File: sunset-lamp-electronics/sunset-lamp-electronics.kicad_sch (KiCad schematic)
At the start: 30 parts

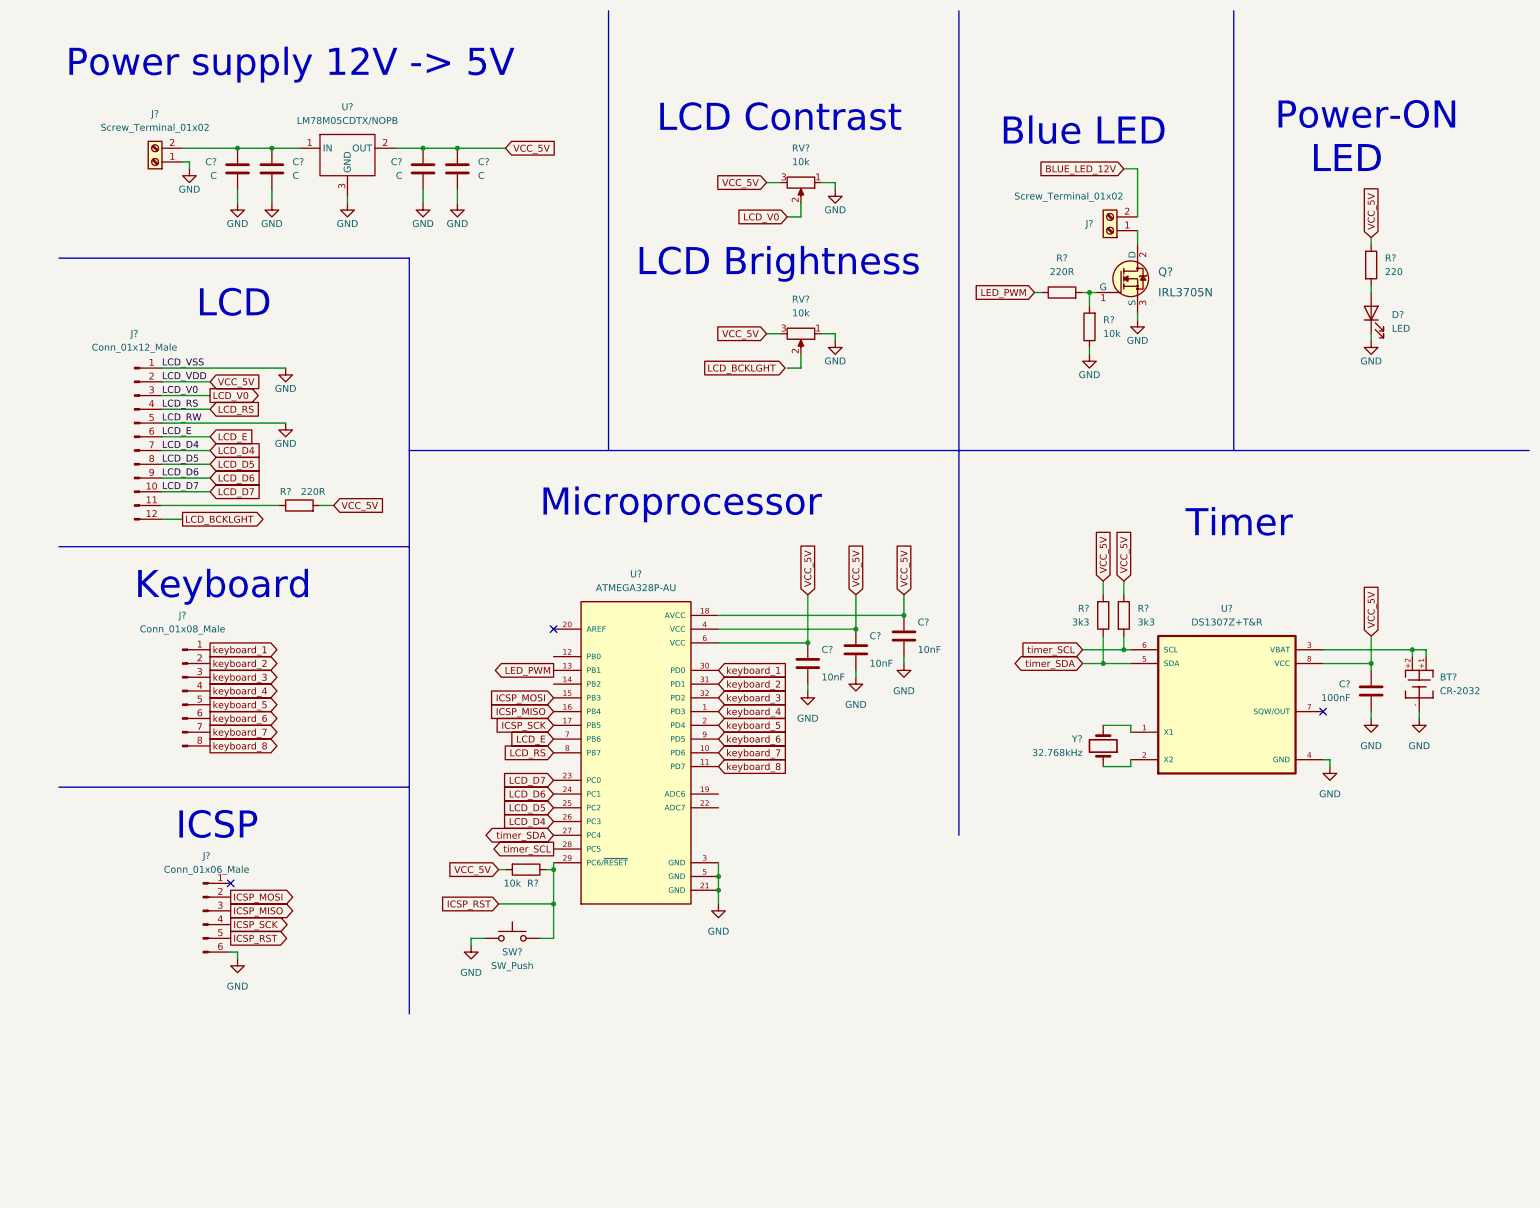
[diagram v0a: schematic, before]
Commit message: Finished schematics and added footprints to all components
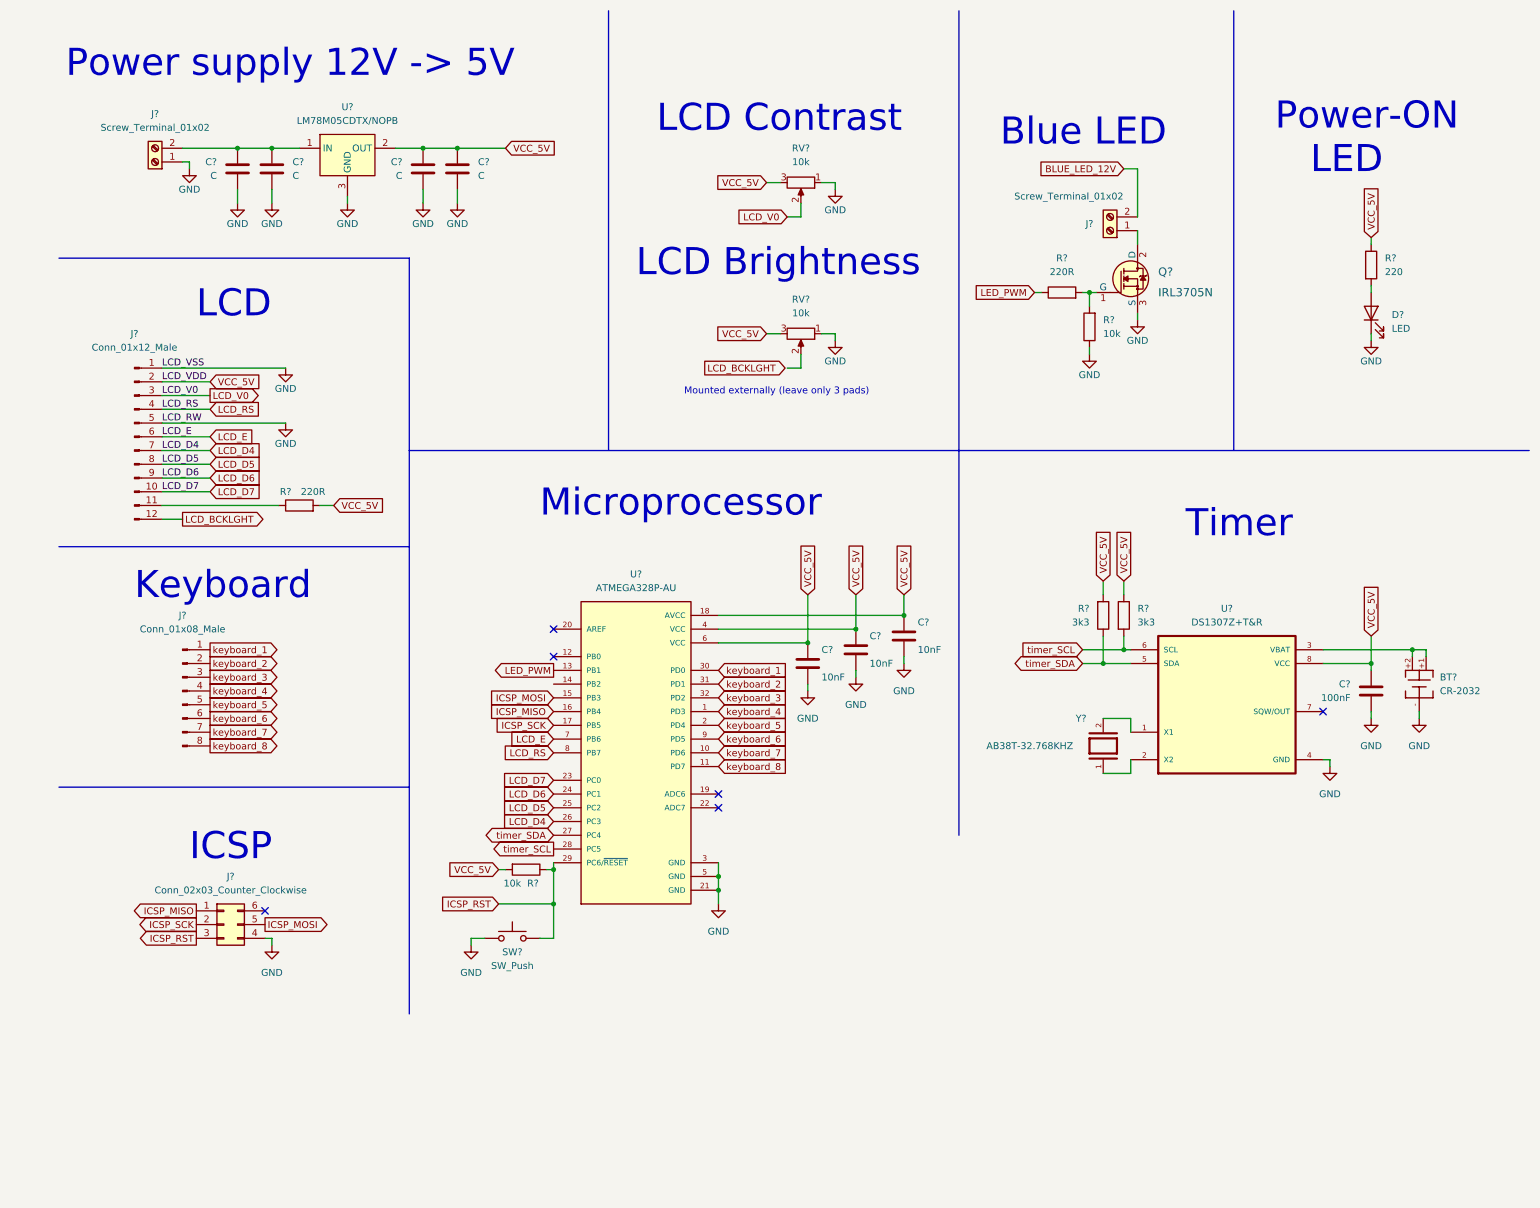
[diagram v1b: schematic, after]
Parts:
- removed J?: Conn_01x06_Male, symbol Connector:Conn_01x06_Male
- removed U?: LM78M05CDTX/NOPB, symbol iridiumLinearVoltageRegulators:LM78M05CDTX/NOPB
- removed Y?: 32.768kHz, symbol Device:Crystal
- added J?: Conn_02x03_Counter_Clockwise, Connector_PinHeader_2.54mm:PinHeader_2x03_P2.54mm_Vertical, symbol Connector_Generic:Conn_02x03_Counter_Clockwise
- added U?: LM78M05CDTX/NOPB, iridium-footprints:TO-252-DPAK, symbol iridiumLinearVoltageRegulators:LM78M05CDTX/NOPB
- added Y?: AB38T-32.768KHZ, iridium-footprints:XTAL_AB38T-32.768KHZ, symbol iridiumOscillators:AB38T-32.768KHZ
- D?: footprint (none) -> LED_SMD:LED_0805_2012Metric_Pad1.15x1.40mm_HandSolder
- J?: footprint (none) -> Connector_PinHeader_2.54mm:PinHeader_1x12_P2.54mm_Vertical
- J? (x2): footprint (none) -> TerminalBlock:TerminalBlock_Altech_AK300-2_P5.00mm
- J?: footprint (none) -> Connector_PinHeader_2.54mm:PinHeader_1x08_P2.54mm_Vertical
- Q?: footprint (none) -> iridium-footprints:TO-220
- RV?: footprint (none) -> iridium-footprints:TrimmPotentiometer
- RV?: footprint (none) -> Connector_PinHeader_2.54mm:PinHeader_1x03_P2.54mm_Vertical
- SW?: footprint (none) -> Button_Switch_THT:SW_PUSH_6mm_H5mm
- U?: footprint QFP80P900X900X120-32N -> iridium-footprints:TQFP-32
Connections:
- net GND: now also J?.4 (Pin_4), U?.3 (GND)
- net ICSP_MISO: now also J?.1 (Pin_1)
- net ICSP_MOSI: now also J?.5 (Pin_5)
- net ICSP_RST: now also J?.3 (Pin_3)
- net ICSP_SCK: now also J?.2 (Pin_2)
- net VCC_5V: now also U?.2 (OUT)
- net at U?.1 (X1): now also Y?.2
- net at U?.2 (X2): now also Y?.1
- net at C?.1, C?.2, J?.2 (Pin_2): now also U?.1 (IN)
- no-connect marks 3 -> 6
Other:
- note added: "Mounted externally (leave only 3 pads)"

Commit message: Corrected R and C symbols and performed ERC
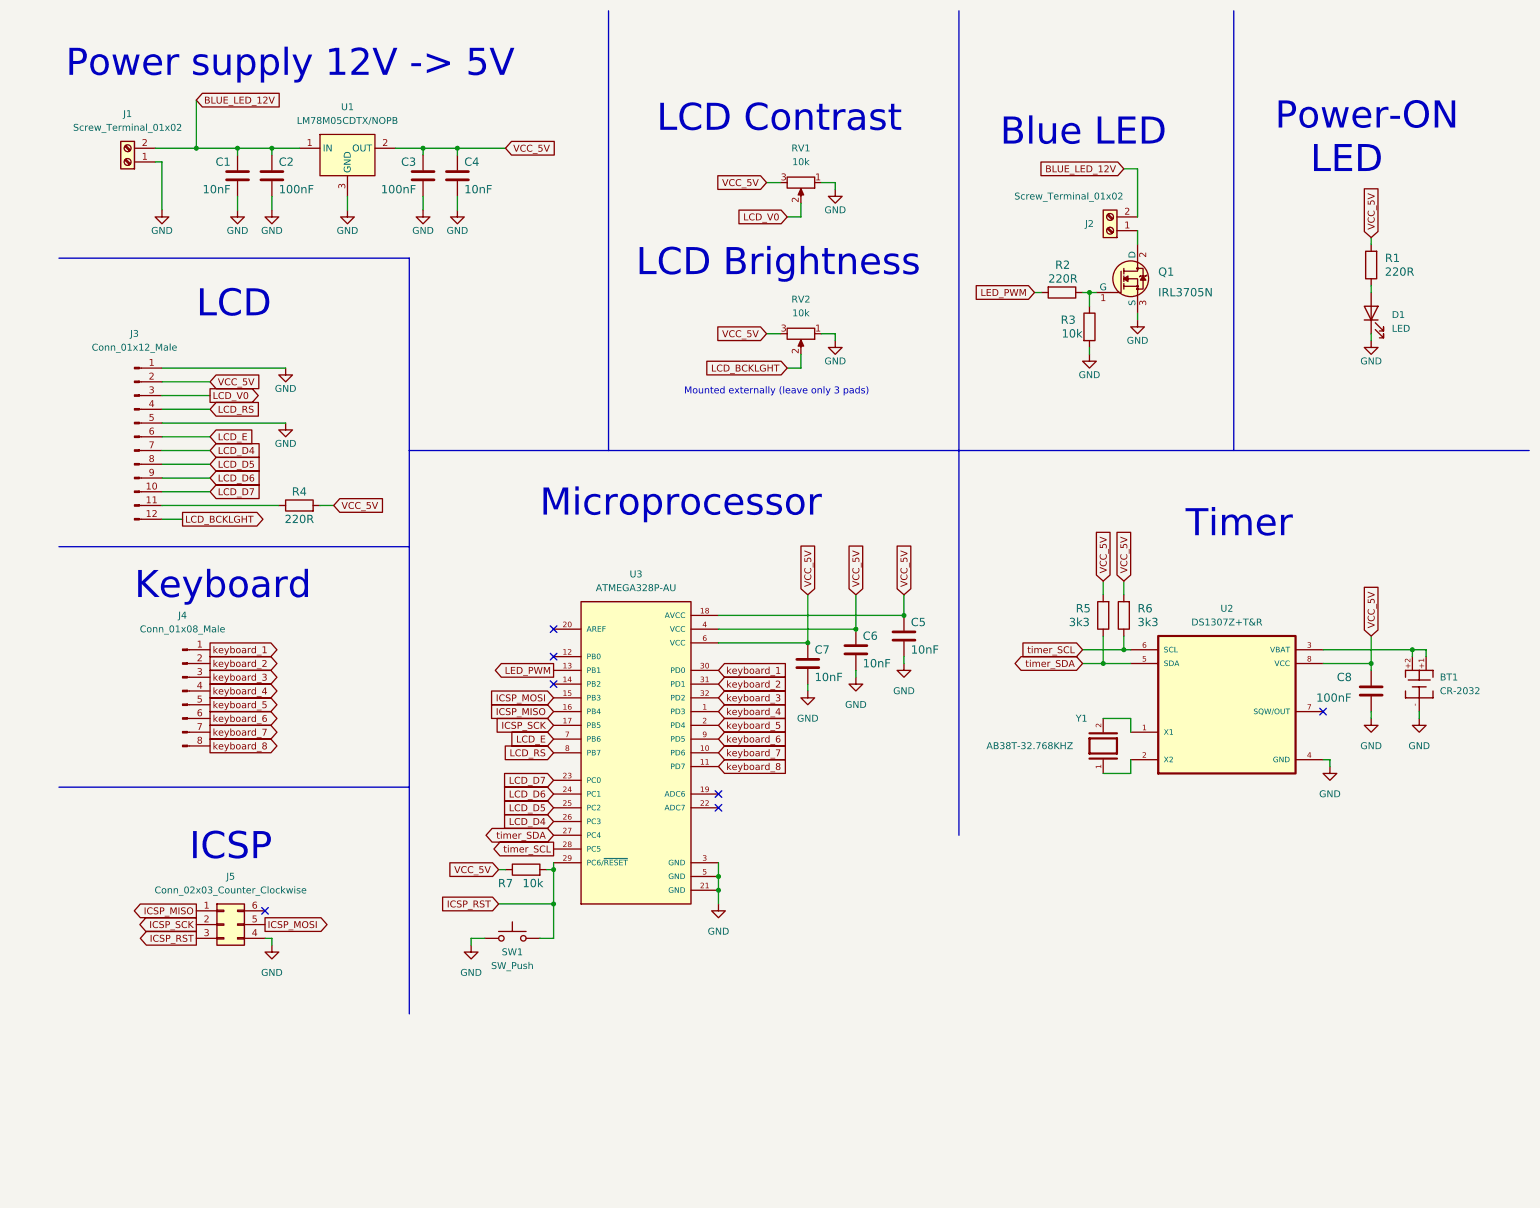
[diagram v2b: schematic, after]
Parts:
- removed C? (x3): 10nF, symbol Device:C
- removed C? (x4): C, symbol Device:C
- removed C?: 100nF, symbol Device:C
- removed R? (x2): 3k3, symbol Device:R
- removed R? (x2): 220R, symbol Device:R
- removed R? (x2): 10k, symbol Device:R
- removed R?: 220, symbol Device:R
- removed U?: ATMEGA328P-AU, iridium-footprints:TQFP-32, symbol iridium-avr:ATMEGA328P-AU
- added C1, C4, C5, C6, C7: 10nF, iridium-footprints:0402-cap, symbol iridiumCapacitorsSMD:C_0402
- added C2, C3, C8: 100nF, iridium-footprints:0402-cap, symbol iridiumCapacitorsSMD:C_0402
- added R1, R2, R4: 220R, iridium-footprints:0402-res, symbol iridiumResistorsSMD:R_0402
- added R3, R7: 10k, iridium-footprints:0402-res, symbol iridiumResistorsSMD:R_0402
- added R5, R6: 3k3, iridium-footprints:0402-res, symbol iridiumResistorsSMD:R_0402
- added U3: ATMEGA328P-AU, iridium-footprints:TQFP-32, symbol iridiumAVR:ATMEGA328P-AU
- gave numbers to parts that had none: 14
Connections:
- net BLUE_LED_12V: now also J1.2 (Pin_2), U1.1 (IN), C1.1, C2.1
- net GND: now also C1.2, C2.2, C3.2, C4.2, C5.2, C6.2, C7.2, C8.2, R3.2, U3.21 (GND), U3.3 (GND), U3.5 (GND)
- net ICSP_MISO: now also U3.16 (PB4)
- net ICSP_MOSI: now also U3.15 (PB3)
- net ICSP_RST: now also R7.2, U3.29 (PC6/~{RESET})
- net ICSP_SCK: now also U3.17 (PB5)
- net LCD_BCKLGHT: now also RV2.2
- net LCD_D4: now also U3.26 (PC3)
- net LCD_D5: now also U3.25 (PC2)
- net LCD_D6: now also U3.24 (PC1)
- net LCD_D7: now also U3.23 (PC0)
- net LCD_E: now also U3.7 (PB6)
- net LCD_RS: now also U3.8 (PB7)
- net LED_PWM: now also R2.2, U3.13 (PB1)
- net VCC_5V: now also C3.1, C4.1, C5.1, C6.1, C7.1, C8.1, R1.2, R4.2, R5.2, R6.2, R7.1, U3.18 (AVCC), U3.4 (VCC), U3.6 (VCC)
- net keyboard_1: now also U3.30 (PD0)
- net keyboard_2: now also U3.31 (PD1)
- net keyboard_3: now also U3.32 (PD2)
- net keyboard_4: now also U3.1 (PD3)
- net keyboard_5: now also U3.2 (PD4)
- net keyboard_6: now also U3.9 (PD5)
- net keyboard_7: now also U3.10 (PD6)
- net keyboard_8: now also U3.11 (PD7)
- net timer_SCL: now also R6.1, U3.28 (PC5)
- net timer_SDA: now also R5.1, U3.27 (PC4)
- net at J3.11 (Pin_11): now also R4.1
- net at Q1.1 (G): now also R2.1, R3.1
- net at D1.2 (A): now also R1.1
- no-connect marks 6 -> 7
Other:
- moved on the sheet: J1

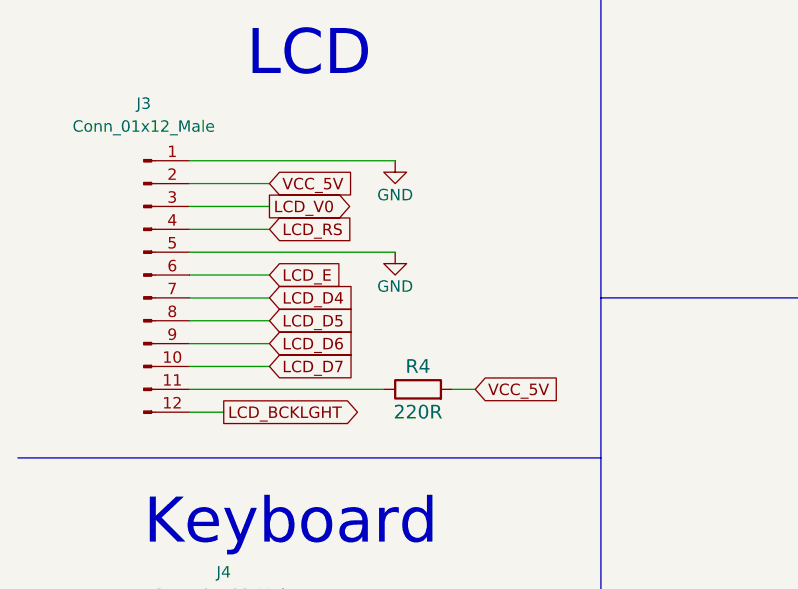
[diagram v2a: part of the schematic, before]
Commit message: Created PCB layout and resolved DRC errors
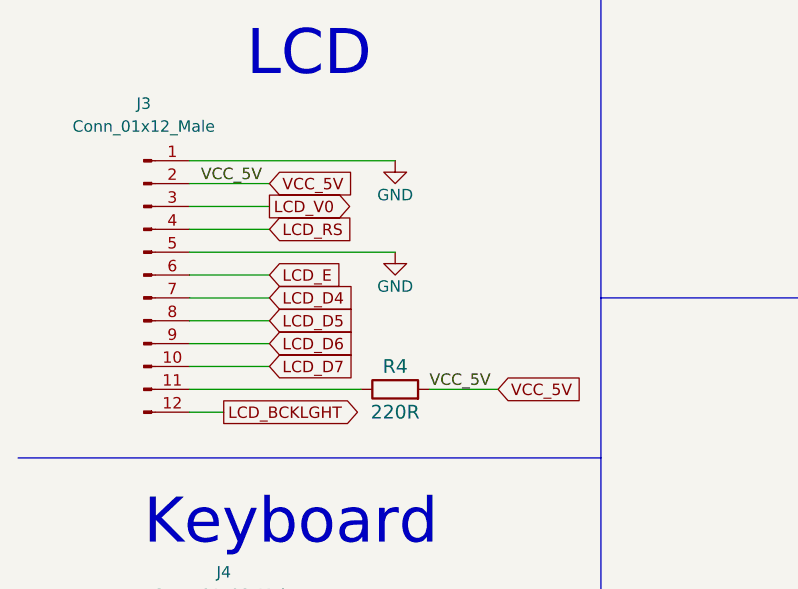
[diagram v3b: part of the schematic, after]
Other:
- moved on the sheet: R4
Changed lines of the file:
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@@
+    (stroke (width 0) (type default) (color 0 0 0 0))
+  )
+  (wire (pts (xy 31.75 104.14) (xy 50.8 104.14))
     (stroke (width 0) (type default) (color 0 0 0 0))
   )
@@
     (stroke (width 0) (type default) (color 0 0 0 0))
   )
-  (wire (pts (xy 31.75 104.14) (xy 53.34 104.14))
-    (stroke (width 0) (type default) (color 0 0 0 0))
-  )
   (polyline (pts (xy 179.07 12.7) (xy 179.07 93.98))
     (stroke (width 0) (type default) (color 0 0 0 0))
@@
     (stroke (width 0) (type default) (color 0 0 0 0))
   )
+  (wire (pts (xy 58.42 104.14) (xy 66.04 104.14))
+    (stroke (width 0) (type default) (color 0 0 0 0))
+  )
   (wire (pts (xy 209.55 41.91) (xy 212.09 41.91))
     (stroke (width 0) (type default) (color 0 0 0 0))
@@
   )
   (wire (pts (xy 143.51 72.39) (xy 146.05 72.39))
-    (stroke (width 0) (type default) (color 0 0 0 0))
-  )
-  (wire (pts (xy 60.96 104.14) (xy 63.5 104.14))
     (stroke (width 0) (type default) (color 0 0 0 0))
   )
@@
     (effects (font (size 1.27 1.27)) (justify left bottom))
   )
+  (label "VCC_5V" (at 33.02 81.28 0)
+    (effects (font (size 1.27 1.27)) (justify left bottom))
+  )
+  (label "VCC_5V" (at 58.42 104.14 0)
+    (effects (font (size 1.27 1.27)) (justify left bottom))
+  )
   (global_label "BLUE_LED_12V" (shape input) (at 209.55 41.91 180) (fields_autoplaced)
     (effects (font (size 1.27 1.27)) (justify right))
@@
     )
   )
-  (global_label "VCC_5V" (shape input) (at 63.5 104.14 0) (fields_autoplaced)
-    (effects (font (size 1.27 1.27)) (justify left))
-    (property "Intersheet References" "${INTERSHEET_REFS}" (id 0) (at 72.8074 104.0606 0)
+  (global_label "VCC_5V" (shape input) (at 66.04 104.14 0) (fields_autoplaced)
+    (effects (font (size 1.27 1.27)) (justify left))
+    (property "Intersheet References" "${INTERSHEET_REFS}" (id 0) (at 75.3474 104.0606 0)
       (effects (font (size 1.27 1.27)) (justify left) hide)
     )
@@
     (pin "2")
   )
-  (symbol (lib_id "iridiumResistorsSMD:R_0402") (at 57.15 104.14 0) (unit 1)
-    (in_bom yes) (on_board yes)
-    (property "Reference" "R4" (id 0) (at 57.15 101.6 0)
+  (symbol (lib_id "iridiumResistorsSMD:R_0402") (at 54.61 104.14 0) (unit 1)
+    (in_bom yes) (on_board yes)
+    (property "Reference" "R4" (id 0) (at 54.61 101.6 0)
       (effects (font (size 1.524 1.524)))
     )
-    (property "Value" "220R" (id 1) (at 57.15 106.68 0)
+    (property "Value" "220R" (id 1) (at 54.61 106.68 0)
       (effects (font (size 1.524 1.524)))
     )
-    (property "Footprint" "iridium-footprints:0402-res" (id 2) (at 62.23 99.06 0)
-      (effects (font (size 1.524 1.524)) (justify left) hide)
-    )
-    (property "Datasheet" "" (id 3) (at 57.15 104.14 0)
-      (effects (font (size 1.27 1.27)) hide)
-    )
-    (property "Manufacturer" "" (id 4) (at 62.23 93.98 0)
-      (effects (font (size 1.524 1.524)) (justify left) hide)
-    )
-    (property "MPN" "" (id 5) (at 62.23 96.52 0)
-      (effects (font (size 1.524 1.524)) (justify left) hide)
-    )
-    (property "Val" "" (id 6) (at 57.15 106.68 0))
-    (pin "1")
-    (pin "2")
+    (property "Footprint" "iridium-footprints:0402-res" (id 2) (at 59.69 99.06 0)
+      (effects (font (size 1.524 1.524)) (justify left) hide)
+    )
+    (property "Datasheet" "" (id 3) (at 54.61 104.14 0)
+      (effects (font (size 1.27 1.27)) hide)
+    )
+    (property "Manufacturer" "" (id 4) (at 59.69 93.98 0)
+      (effects (font (size 1.524 1.524)) (justify left) hide)
+    )
+    (property "MPN" "" (id 5) (at 59.69 96.52 0)
+      (effects (font (size 1.524 1.524)) (justify left) hide)
+    )
+    (property "Val" "" (id 6) (at 54.61 106.68 0))
+    (pin "1")
+    (pin "2")
